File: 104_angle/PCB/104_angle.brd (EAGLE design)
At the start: 25.4 x 33 mm, 4 parts, among them U1 ANGLE

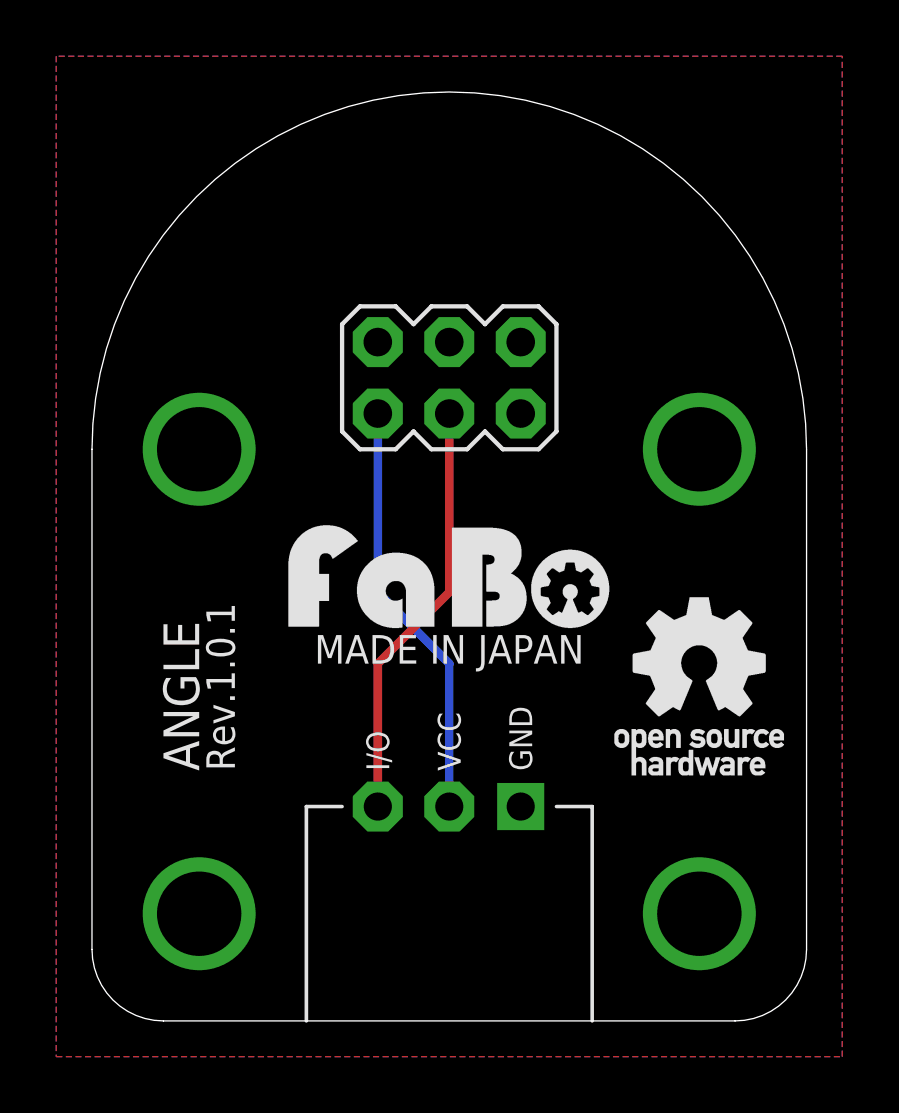
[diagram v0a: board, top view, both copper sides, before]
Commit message: add product number
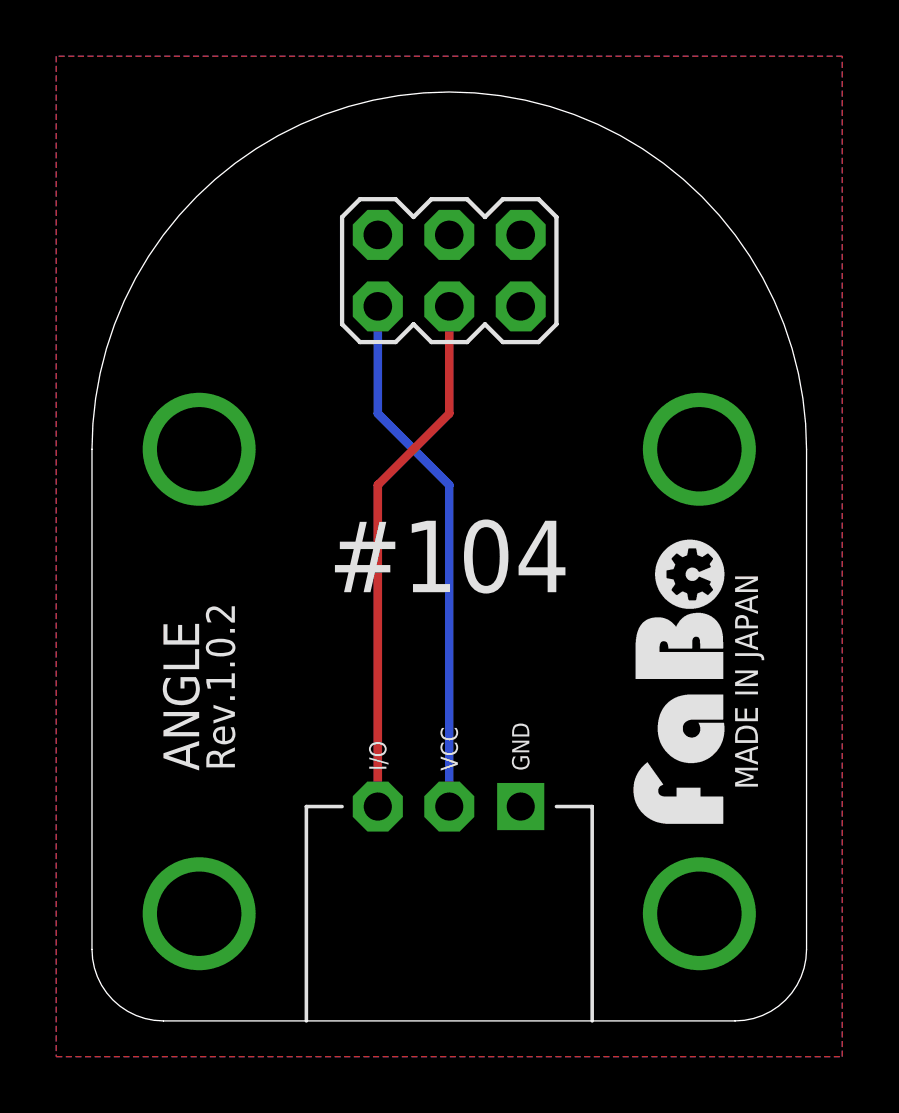
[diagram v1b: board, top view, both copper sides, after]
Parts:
- U$2: device FaBo-etc:LOGO_FABO_M -> FaBo-etc:LOGO_FABO_MS
- U$3: device FaBo-etc:LOGO_OSHW_T_M -> FaBo-etc:LOGO_OSHW_T_MS_BOTTOM
- moved U$3 12.6 mm to (12.7, 3.81)
- moved U$2 10.3 mm to (22.9, 12.1), turned to 90 degrees
- moved U1 3.81 mm to (12.7, 26.7)
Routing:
- net VCC: track 15.0 -> 18.8 mm
- net N$1: track 15.0 -> 18.8 mm
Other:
- board text added: "#104"
- board text added: "Rev.1.0.2"
- board text removed: "Rev.1.0.1"
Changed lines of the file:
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@@
 <plain>
 <text x="3.81" y="8.89" size="1.27" layer="21" font="vector" ratio="12" rot="R90">ANGLE</text>
-<text x="5.08" y="8.89" size="1.016" layer="21" font="vector" ratio="12" rot="R90">Rev.1.0.1</text>
-<text x="12.7" y="12.7" size="1.016" layer="21" font="vector" ratio="12" align="bottom-center">MADE IN JAPAN</text>
+<text x="5.08" y="8.89" size="1.016" layer="21" font="vector" ratio="12" rot="R90">Rev.1.0.2</text>
+<text x="22.86" y="12.065" size="0.8128" layer="21" font="vector" ratio="12" rot="R270" align="bottom-center">MADE IN JAPAN</text>
+<text x="12.7" y="15.24" size="2.54" layer="21" font="vector" ratio="12" align="bottom-center">#104</text>
 </plain>
 <attributes>
@@
 </autorouter>
 <elements>
-<element name="U1" library="FaBo-etc" package="ROTARYENCORDER_BRICK" value="ANGLE" x="12.7" y="22.86"/>
+<element name="U1" library="FaBo-etc" package="ROTARYENCORDER_BRICK" value="ANGLE" x="12.7" y="26.67"/>
 <element name="J1" library="FaBo-Template" package="FABO_BRICK_3PIN" value="" x="12.7" y="16.51"/>
-<element name="U$2" library="FaBo-etc" package="LOGO_FABO_M" value="" x="12.7" y="13.97"/>
-<element name="U$3" library="FaBo-etc" package="LOGO_OSHW_T_M" value="" x="21.59" y="12.7"/>
+<element name="U$2" library="FaBo-etc" package="LOGO_FABO_MS" value="" x="22.86" y="12.065" rot="R90"/>
+<element name="U$3" library="FaBo-etc" package="LOGO_OSHW_T_MS_BOTTOM" value="" x="12.7" y="3.81"/>
 </elements>
 <signals>
@@
 <contactref element="J1" pad="VCC"/>
 <contactref element="U1" pad="1"/>
-<wire x1="10.16" y1="21.59" x2="10.16" y2="15.24" width="0.3048" layer="16"/>
-<wire x1="10.16" y1="15.24" x2="12.7" y2="12.7" width="0.3048" layer="16"/>
-<wire x1="12.7" y1="12.7" x2="12.7" y2="7.62" width="0.3048" layer="16"/>
+<wire x1="10.16" y1="25.4" x2="10.16" y2="21.59" width="0.3048" layer="16"/>
+<wire x1="10.16" y1="21.59" x2="12.7" y2="19.05" width="0.3048" layer="16"/>
+<wire x1="12.7" y1="19.05" x2="12.7" y2="7.62" width="0.3048" layer="16"/>
 </signal>
 <signal name="GND">
@@
 <contactref element="J1" pad="IN/OUT"/>
 <contactref element="U1" pad="3"/>
-<wire x1="12.7" y1="21.59" x2="12.7" y2="15.24" width="0.3048" layer="1"/>
-<wire x1="12.7" y1="15.24" x2="10.16" y2="12.7" width="0.3048" layer="1"/>
-<wire x1="10.16" y1="12.7" x2="10.16" y2="7.62" width="0.3048" layer="1"/>
+<wire x1="12.7" y1="25.4" x2="12.7" y2="21.59" width="0.3048" layer="1"/>
+<wire x1="12.7" y1="21.59" x2="10.16" y2="19.05" width="0.3048" layer="1"/>
+<wire x1="10.16" y1="19.05" x2="10.16" y2="7.62" width="0.3048" layer="1"/>
 </signal>
 </signals>

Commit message: fix solder land(non-check)
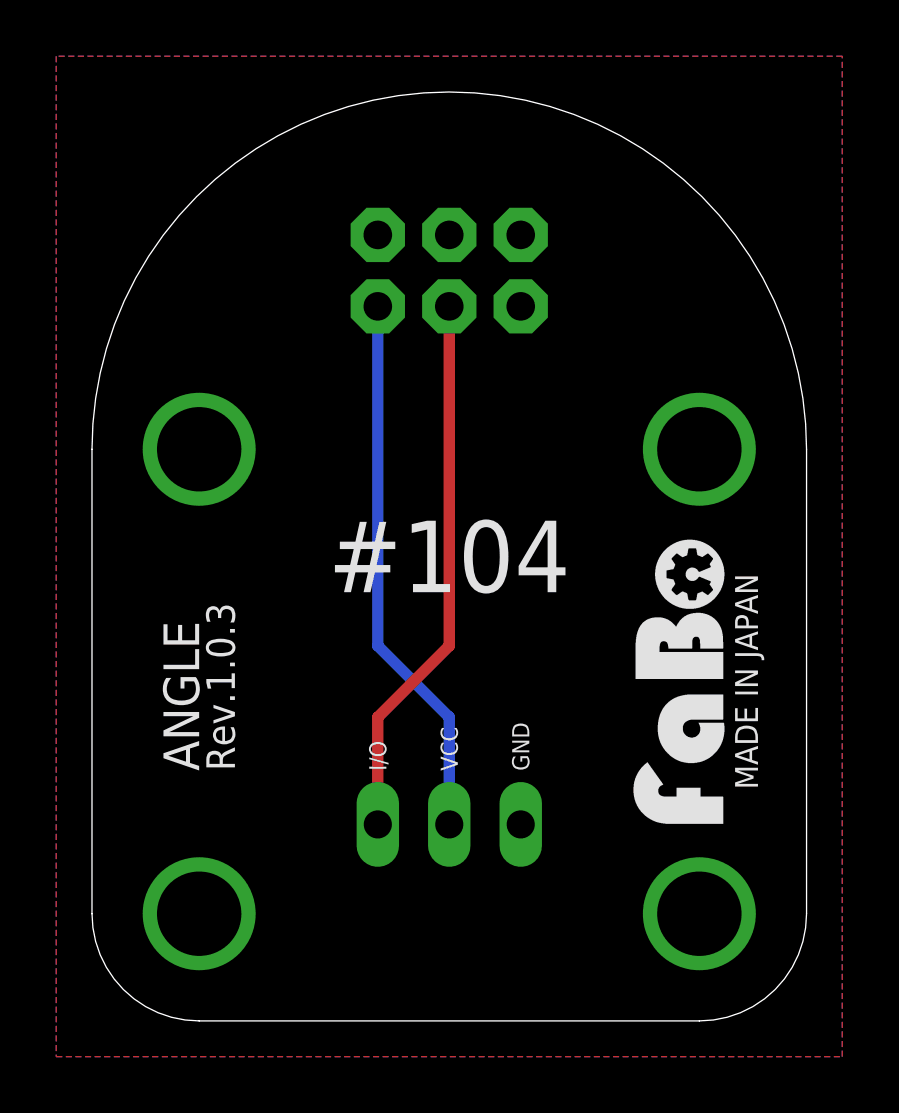
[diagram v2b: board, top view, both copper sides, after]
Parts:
- U1: value ANGLE -> (none); device FaBo-etc:ROTARYENCORDER_BRICK -> FaBo-Parts:ROTARYENCORDER
- moved U$3 0.38 mm to (12.7, 3.43)
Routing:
- net VCC: track 18.8 -> 19.5 mm
- net N$1: track 18.8 -> 19.5 mm
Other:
- outline, holes or cut-outs redrawn
- board text added: "Rev.1.0.3"
- board text removed: "Rev.1.0.2"
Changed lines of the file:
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@@
 <?xml version="1.0" encoding="utf-8"?>
 <!DOCTYPE eagle SYSTEM "eagle.dtd">
-<eagle version="7.4.0">
+<eagle version="7.5.0">
 <drawing>
 <settings>
@@
 <setting verticaltext="up"/>
 </settings>
-<grid distance="0.05" unitdist="inch" unit="inch" style="lines" multiple="1" display="yes" altdistance="0.025" altunitdist="inch" altunit="inch"/>
+<grid distance="25" unitdist="mil" unit="mil" style="lines" multiple="1" display="yes" altdistance="0.025" altunitdist="inch" altunit="inch"/>
 <layers>
 <layer number="1" name="Top" color="4" fill="1" visible="yes" active="yes"/>
@@
 <plain>
 <text x="3.81" y="8.89" size="1.27" layer="21" font="vector" ratio="12" rot="R90">ANGLE</text>
-<text x="5.08" y="8.89" size="1.016" layer="21" font="vector" ratio="12" rot="R90">Rev.1.0.2</text>
+<text x="5.08" y="8.89" size="1.016" layer="21" font="vector" ratio="12" rot="R90">Rev.1.0.3</text>
 <text x="22.86" y="12.065" size="0.8128" layer="21" font="vector" ratio="12" rot="R270" align="bottom-center">MADE IN JAPAN</text>
-<text x="12.7" y="15.24" size="2.54" layer="21" font="vector" ratio="12" align="bottom-center">#104</text>
+<text x="12.7" y="16.51" size="2.54" layer="21" font="vector" ratio="12" align="center">#104</text>
 </plain>
 <attributes>
@@
 </autorouter>
 <elements>
-<element name="U1" library="FaBo-etc" package="ROTARYENCORDER_BRICK" value="ANGLE" x="12.7" y="26.67"/>
 <element name="J1" library="FaBo-Template" package="FABO_BRICK_3PIN" value="" x="12.7" y="16.51"/>
 <element name="U$2" library="FaBo-etc" package="LOGO_FABO_MS" value="" x="22.86" y="12.065" rot="R90"/>
-<element name="U$3" library="FaBo-etc" package="LOGO_OSHW_T_MS_BOTTOM" value="" x="12.7" y="3.81"/>
+<element name="U$3" library="FaBo-etc" package="LOGO_OSHW_T_MS_BOTTOM" value="" x="12.7" y="3.429"/>
+<element name="U1" library="FaBo-Parts" package="ROTARYENCORDER" value="" x="12.7" y="26.67"/>
 </elements>
 <signals>
@@
 <contactref element="J1" pad="VCC"/>
 <contactref element="U1" pad="1"/>
-<wire x1="10.16" y1="25.4" x2="10.16" y2="21.59" width="0.3048" layer="16"/>
-<wire x1="10.16" y1="21.59" x2="12.7" y2="19.05" width="0.3048" layer="16"/>
-<wire x1="12.7" y1="19.05" x2="12.7" y2="7.62" width="0.3048" layer="16"/>
+<wire x1="10.16" y1="25.4" x2="10.16" y2="13.335" width="0.4064" layer="16"/>
+<wire x1="10.16" y1="13.335" x2="12.7" y2="10.795" width="0.4064" layer="16"/>
+<wire x1="12.7" y1="10.795" x2="12.7" y2="6.985" width="0.4064" layer="16"/>
 </signal>
 <signal name="GND">
 <contactref element="J1" pad="GND"/>
 <contactref element="U1" pad="5"/>
-<polygon width="0.3048" layer="16" spacing="0.3048">
+<polygon width="0.2032" layer="16" spacing="0.254">
 <vertex x="-1.27" y="-1.27"/>
 <vertex x="26.67" y="-1.27"/>
@@
 <vertex x="-1.27" y="34.29"/>
 </polygon>
-<polygon width="0.3048" layer="1" spacing="0.3048">
+<polygon width="0.2032" layer="1" spacing="0.254">
 <vertex x="-1.27" y="-1.27"/>
 <vertex x="26.67" y="-1.27"/>
@@
 <contactref element="J1" pad="IN/OUT"/>
 <contactref element="U1" pad="3"/>
-<wire x1="12.7" y1="25.4" x2="12.7" y2="21.59" width="0.3048" layer="1"/>
-<wire x1="12.7" y1="21.59" x2="10.16" y2="19.05" width="0.3048" layer="1"/>
-<wire x1="10.16" y1="19.05" x2="10.16" y2="7.62" width="0.3048" layer="1"/>
+<wire x1="12.7" y1="25.4" x2="12.7" y2="13.335" width="0.4064" layer="1"/>
+<wire x1="12.7" y1="13.335" x2="10.16" y2="10.795" width="0.4064" layer="1"/>
+<wire x1="10.16" y1="10.795" x2="10.16" y2="6.985" width="0.4064" layer="1"/>
 </signal>
 </signals>

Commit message: fix solder land size
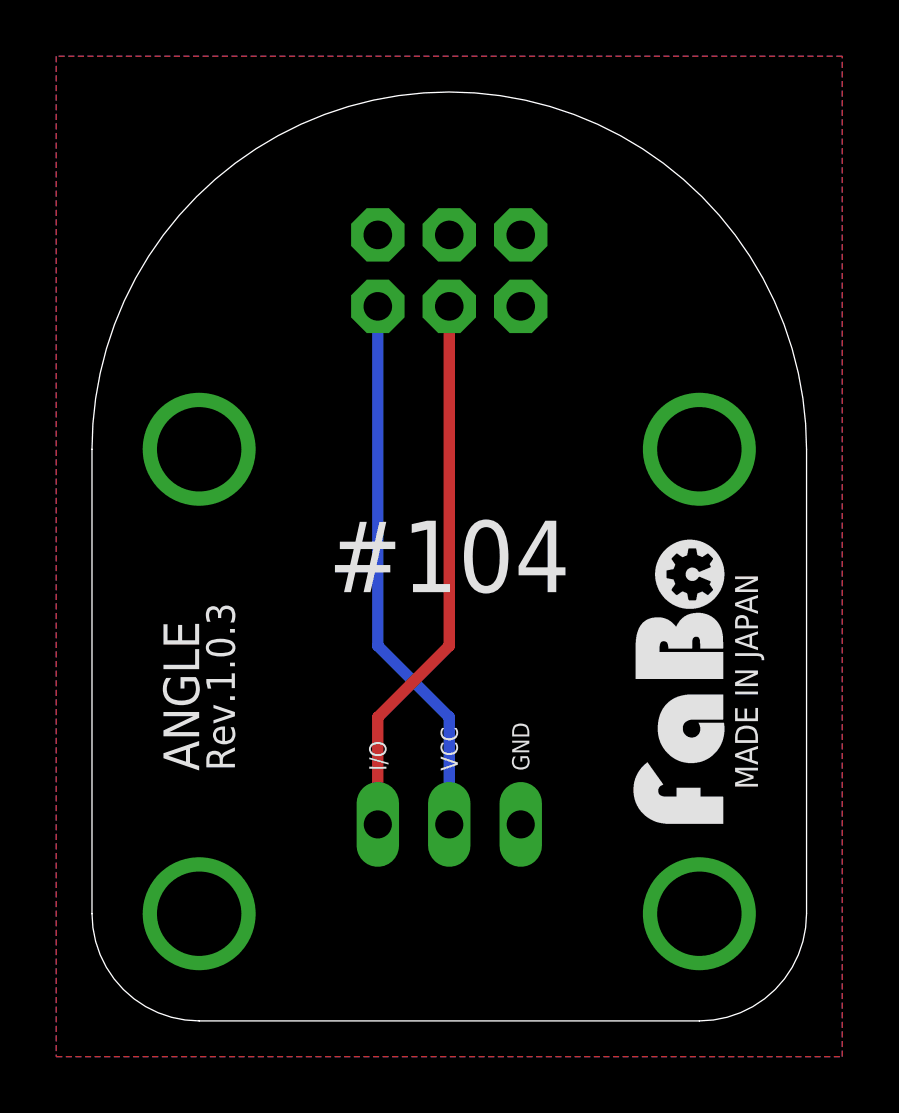
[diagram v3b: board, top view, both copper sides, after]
